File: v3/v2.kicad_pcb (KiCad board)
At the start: 2 copper layers, 82 parts, among them J1 Conn_01x05_Pin, SW1 SW_Push, SW10 SW_Push, SW11 SW_Push, SW12 SW_Push, SW13 SW_Push, SW14 SW_Push, SW15 SW_Push, SW16 SW_Push, SW17 SW_Push, SW18 SW_Push, SW19 SW_Push, SW2 SW_Push, SW20 SW_Push, SW21 SW_Push, SW22 SW_Push, SW23 SW_Push, SW24 SW_Push, SW25 SW_Push, SW26 SW_Push, SW27 SW_Push, SW28 SW_Push, SW29 SW_Push, SW3 SW_Push, SW30 SW_Push, SW31 SW_Push, SW32 SW_Push, SW33 RotaryEncoder_Switch, SW4 SW_Push, SW5 SW_Push, SW6 SW_Push, SW7 SW_Push, SW8 SW_Push, SW9 SW_Push, U1 nice_nano_left

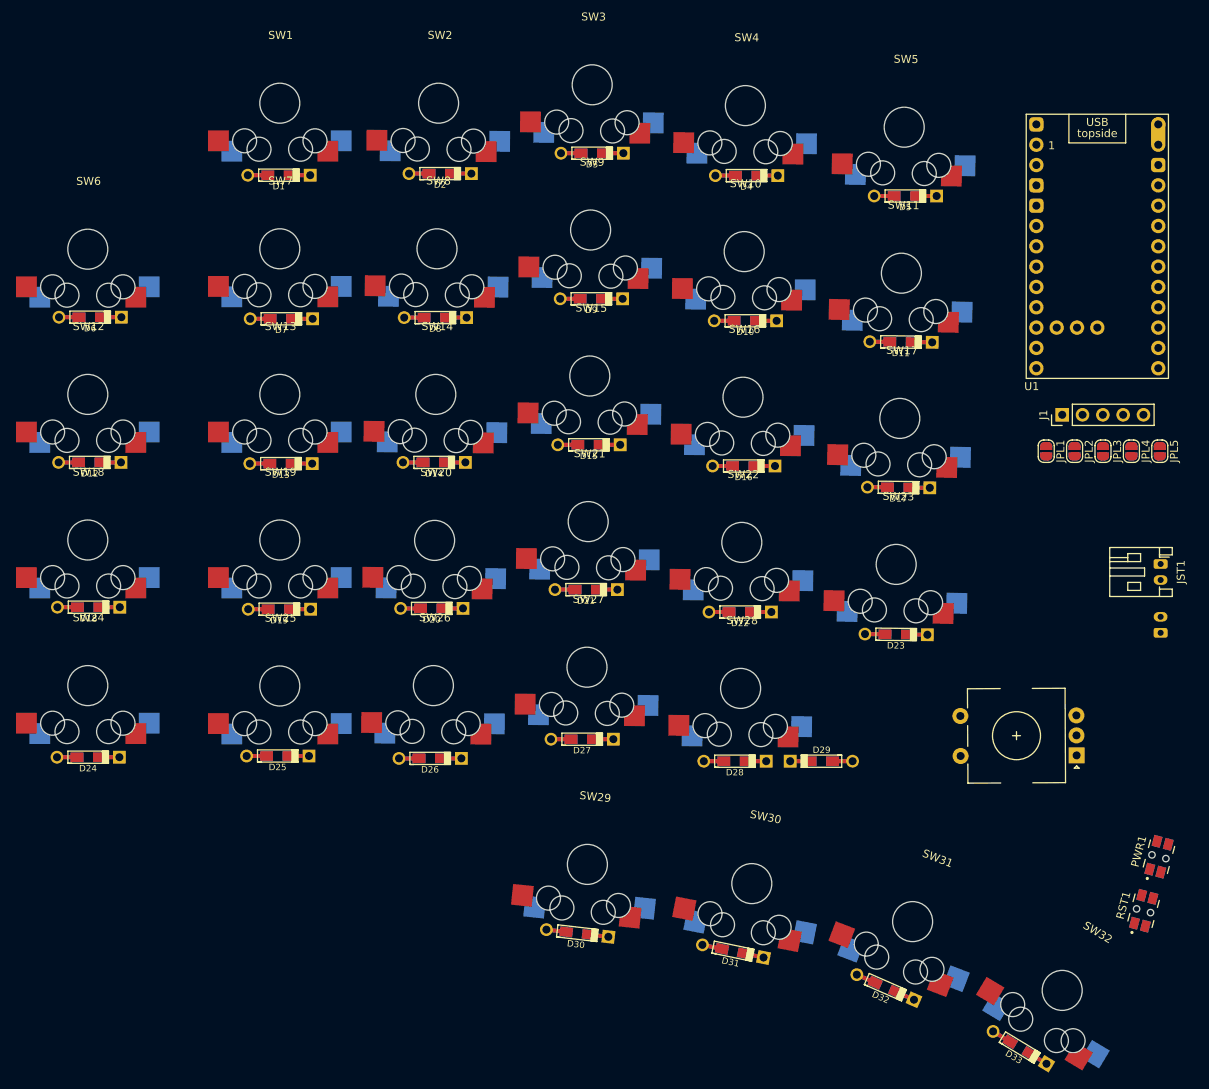
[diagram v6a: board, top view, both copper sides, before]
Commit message: finish routing all traces
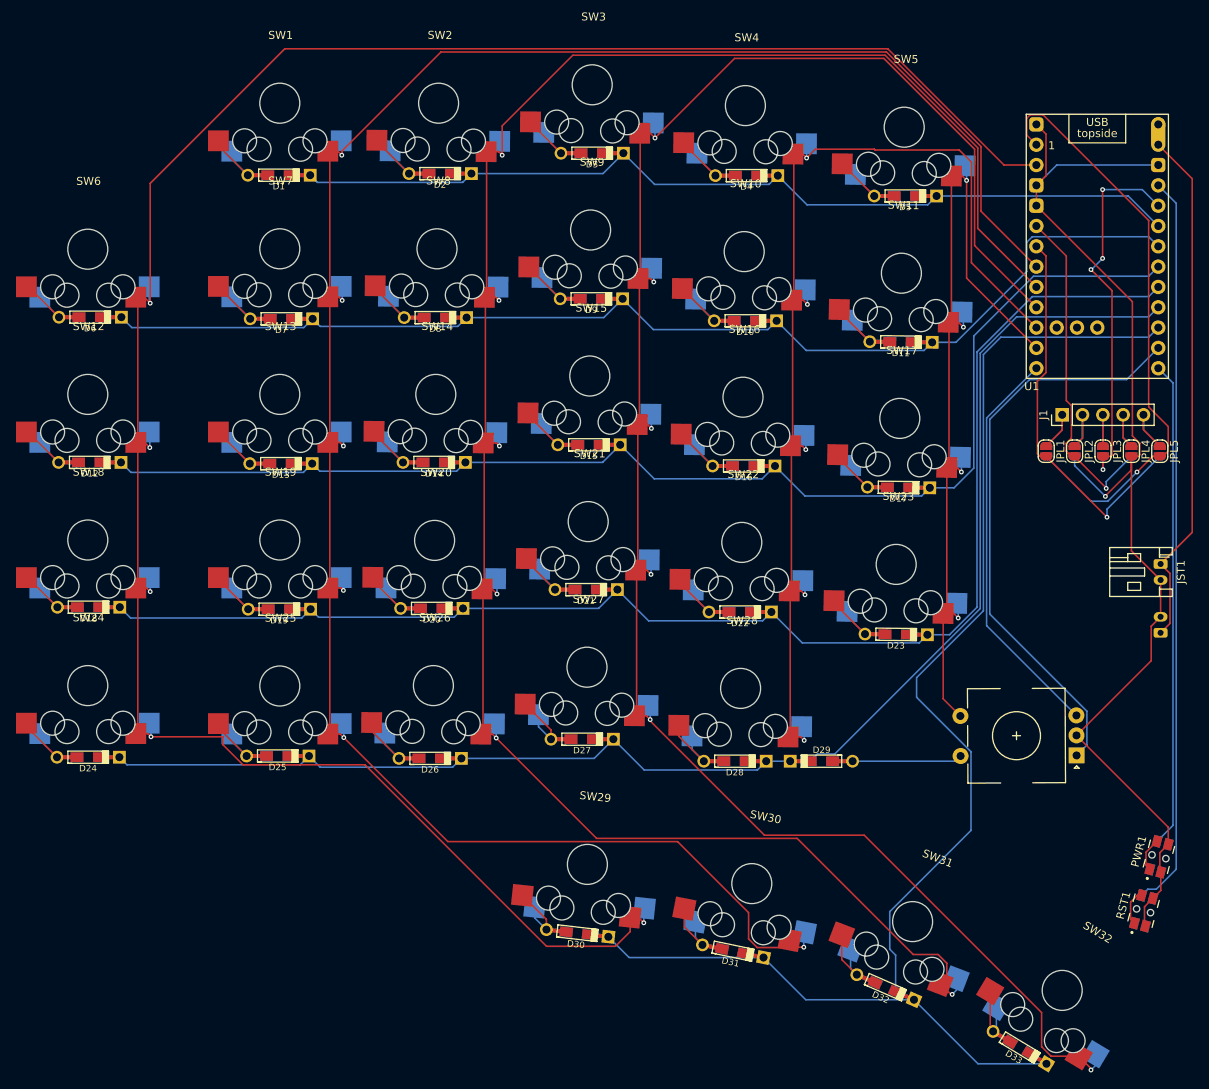
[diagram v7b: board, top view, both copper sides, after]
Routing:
- net Col 1: track 0.00 -> 287.5 mm, vias 0 -> 5
- net Col 2: track 0.00 -> 274.4 mm, vias 0 -> 6
- net Col 3: track 0.00 -> 260.3 mm, vias 0 -> 6
- net Col 4: track 0.00 -> 243.3 mm, vias 0 -> 6
- net Row 6: track 0.00 -> 175.0 mm
- net Row 5: track 0.00 -> 174.5 mm
- net Row 4: track 0.00 -> 173.5 mm
- net Row 3: track 0.00 -> 157.9 mm
- net GND: track 0.00 -> 148.7 mm, vias 0 -> 1
- net Row 2: track 0.00 -> 144.5 mm
- net Col 5: track 0.00 -> 139.1 mm, vias 0 -> 5
- net Row 1: track 0.00 -> 113.5 mm
- net Col 6: track 0.00 -> 109.6 mm, vias 0 -> 4
- net RST: track 0.00 -> 96.7 mm
- net CS: track 0.00 -> 74.7 mm, vias 0 -> 1
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
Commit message: silkscreen
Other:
- board text added: "+"
- board text added: "-"
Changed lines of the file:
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@@
 		(layer "Dwgs.User")
+	)
+	(gr_text "-"
+		(at 269.95 110.9 -0)
+		(layer "B.SilkS")
+		(effects
+			(font
+				(size 1 1)
+				(thickness 0.1)
+			)
+			(justify left bottom mirror)
+		)
+	)
+	(gr_text "-"
+		(at 269.95 115.5 -0)
+		(layer "B.SilkS")
+		(effects
+			(font
+				(size 1 1)
+				(thickness 0.1)
+			)
+			(justify left bottom mirror)
+		)
+	)
+	(gr_text "+"
+		(at 270.038094 108.2 -0)
+		(layer "B.SilkS")
+		(effects
+			(font
+				(size 1 1)
+				(thickness 0.1)
+			)
+			(justify left bottom mirror)
+		)
+	)
+	(gr_text "+"
+		(at 270.038094 117.65 -0)
+		(layer "B.SilkS")
+		(effects
+			(font
+				(size 1 1)
+				(thickness 0.1)
+			)
+			(justify left bottom mirror)
+		)
+	)
+	(gr_text "+"
+		(at 268.7 117.65 0)
+		(layer "F.SilkS")
+		(effects
+			(font
+				(size 1 1)
+				(thickness 0.1)
+			)
+			(justify left bottom)
+		)
+	)
+	(gr_text "+"
+		(at 268.7 108.2 0)
+		(layer "F.SilkS")
+		(effects
+			(font
+				(size 1 1)
+				(thickness 0.1)
+			)
+			(justify left bottom)
+		)
+	)
+	(gr_text "-"
+		(at 268.65 115.5 0)
+		(layer "F.SilkS")
+		(effects
+			(font
+				(size 1 1)
+				(thickness 0.1)
+			)
+			(justify left bottom)
+		)
+	)
+	(gr_text "-"
+		(at 268.6 110.9 0)
+		(layer "F.SilkS")
+		(effects
+			(font
+				(size 1 1)
+				(thickness 0.1)
+			)
+			(justify left bottom)
+		)
 	)
 	(segment
